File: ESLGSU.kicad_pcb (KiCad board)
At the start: 2 copper layers, 1 part

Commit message: Started work on system power section
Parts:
- added C1: 1n, Capacitor_SMD:C_0603_1608Metric, F.Cu at (144.4, 69.7)
- added C10: 100n, Capacitor_SMD:C_0603_1608Metric, F.Cu at (167.1, 69.5)
- added C11: 100n, Capacitor_SMD:C_0603_1608Metric, F.Cu at (171.1, 62.0)
- added C2: 1u, Capacitor_SMD:C_0603_1608Metric, F.Cu at (144.4, 72.2)
- added C3: 22n, Capacitor_SMD:C_0603_1608Metric, F.Cu at (163.1, 62.0)
- added C4: 100n, Capacitor_SMD:C_0603_1608Metric, F.Cu at (163.1, 64.5)
- added C5: 100n, Capacitor_SMD:C_0603_1608Metric, F.Cu at (163.1, 67.0)
- added C6: 100n, Capacitor_SMD:C_0603_1608Metric, F.Cu at (163.1, 69.5)
- added C7: 1u, Capacitor_SMD:C_0603_1608Metric, F.Cu at (167.1, 62.0)
- added C8: 1n, Capacitor_SMD:C_0603_1608Metric, F.Cu at (167.1, 64.5)
- added C9: 22n, Capacitor_SMD:C_0603_1608Metric, F.Cu at (167.1, 67.0)
- added R1: 10K, Resistor_SMD:R_0603_1608Metric, F.Cu at (171.1, 64.5)
- added R2: 5m, Resistor_SMD:R_0603_1608Metric, F.Cu at (171.1, 67.0)
- added R3: 10K, Resistor_SMD:R_0603_1608Metric, F.Cu at (171.1, 69.5)
- added U2: DML3012LDC, Package_DFN_QFN:WDFN-12-1EP_3x3mm_P0.45mm_EP1.7x2.5mm, F.Cu at (149.0, 70.8)
- added U3: LM74700, Package_TO_SOT_SMD:SOT-23-6, F.Cu at (158.5, 63.0)
- added U4: ~, ESLGSU_Parts_Lib:V-DFN3030-8, F.Cu at (163.3, 73.0)
- added U5: INA219AxDCN, Package_TO_SOT_SMD:SOT-23-8, F.Cu at (158.5, 67.4)
- added U6: DML3012LDC, Package_DFN_QFN:WDFN-12-1EP_3x3mm_P0.45mm_EP1.7x2.5mm, F.Cu at (168.2, 73.0)
- added U7: ~, ESLGSU_Parts_Lib:V-DFN3030-8, F.Cu at (163.3, 77.6)
- added U8: LM74700, Package_TO_SOT_SMD:SOT-23-6, F.Cu at (158.5, 71.9)
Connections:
- U1 pad 11: /Pi_Zero/PI_SS_MISC2_IO2 -> /Pi_Zero/PI_RESET_MAIN
- U1 pad 12: unconnected-(U1-GPIO18-Pad12) -> /Pi_Zero/PI_BOOT0_MAIN
- U1 pad 13: /Pi_Zero/PI_RESET_MISC2_IO4 -> /Pi_Zero/PI_BOOT0_MISC2_IO6
- U1 pad 15: /Pi_Zero/PI_BOOT0_MISC2_IO6 -> /Pi_Zero/PI_SS_MISC1_IO1
- U1 pad 16: unconnected-(U1-GPIO23-Pad16) -> /Pi_Zero/PI_RESET_MISC1_IO3
- U1 pad 18: unconnected-(U1-GPIO24-Pad18) -> /Pi_Zero/PI_BOOT0_MISC1_IO5
- U1 pad 22: /Pi_Zero/PI_SS_MISC1_IO1 -> /Pi_Zero/PI_SS_MISC2_IO2
- U1 pad 24: /Pi_Zero/PI_RESET_MISC1_IO3 -> unconnected-(U1-GPIO8-Pad24)
- U1 pad 26: /Pi_Zero/PI_BOOT0_MISC1_IO5 -> unconnected-(U1-GPIO7-Pad26)
- U1 pad 33: /Pi_Zero/PI_SS_MAIN -> unconnected-(U1-GPIO13_PWM1-Pad33)
- U1 pad 35: /Pi_Zero/PI_RESET_MAIN -> /Pi_Zero/PI_SS_EPS
- U1 pad 36: /Pi_Zero/PI_SS_EPS -> /Pi_Zero/PI_SS_MAIN
- U1 pad 37: /Pi_Zero/PI_BOOT0_MAIN -> /Pi_Zero/PI_RESET_MISC2_IO4

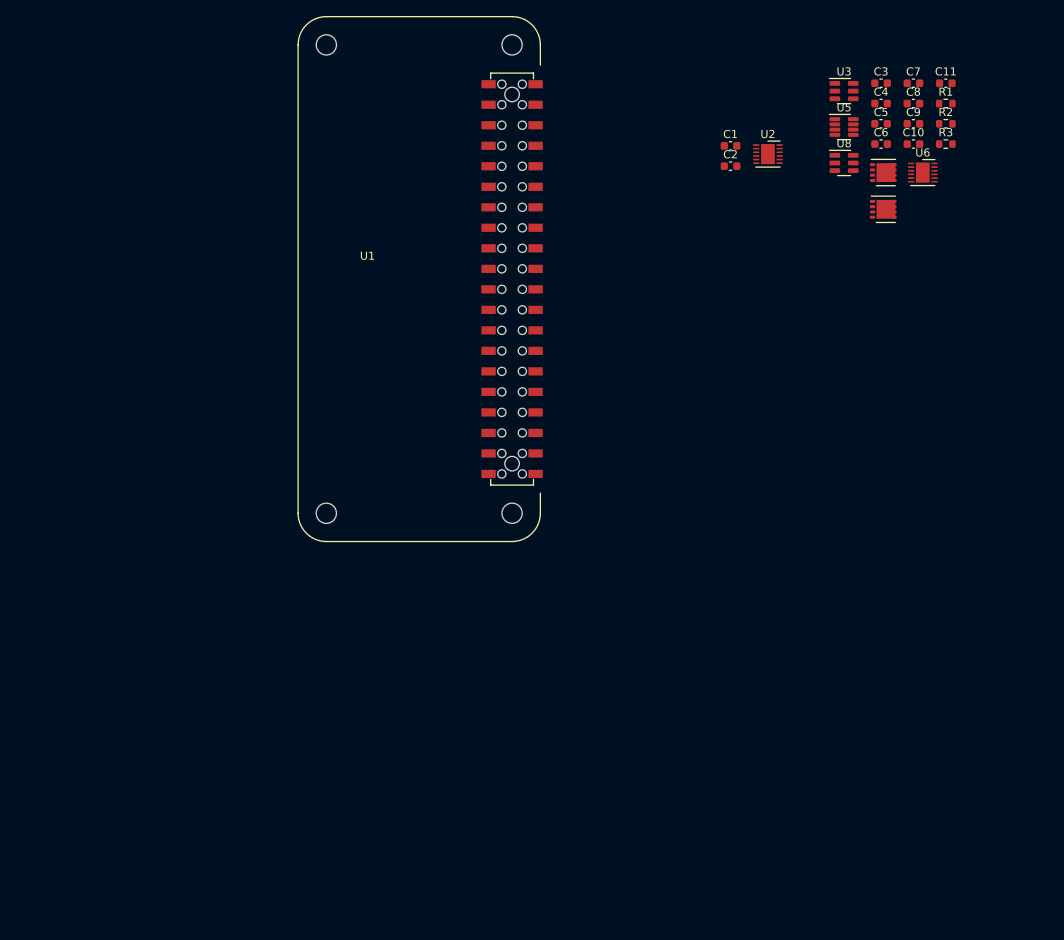
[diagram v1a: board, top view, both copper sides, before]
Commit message: Additional power regulation work
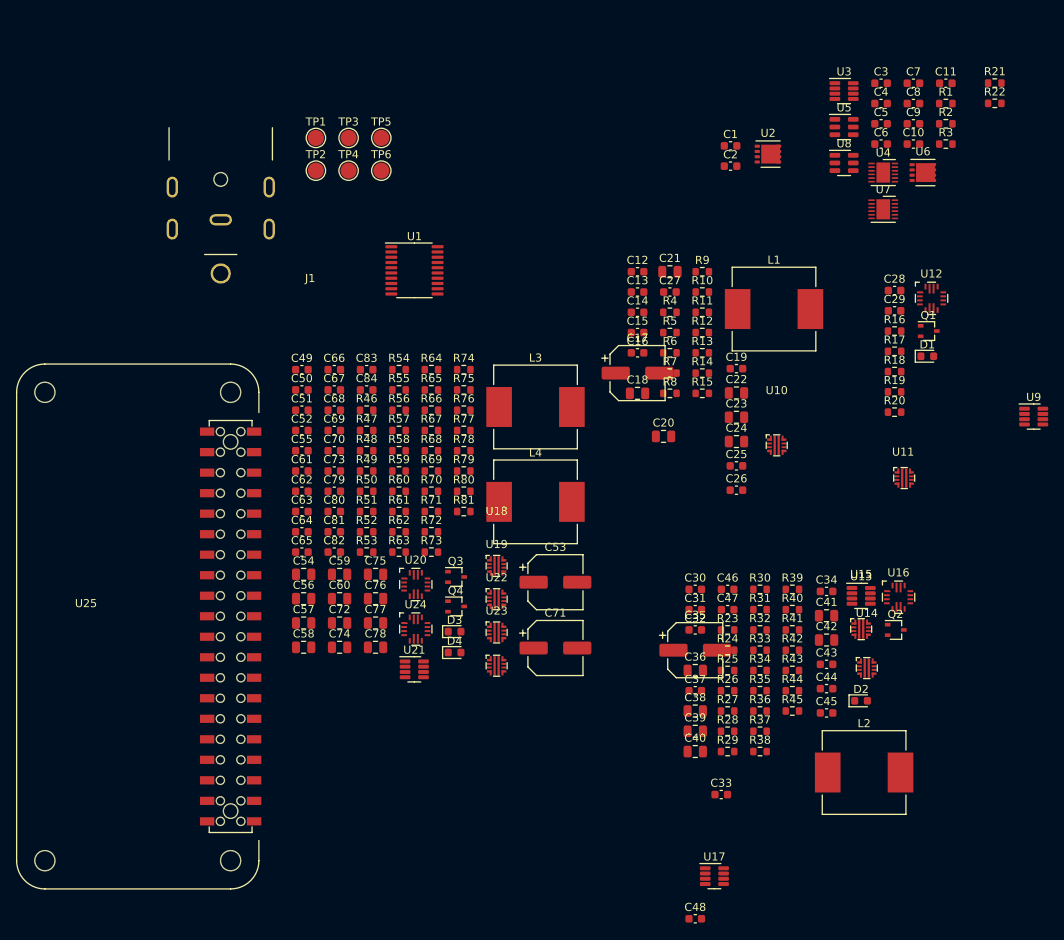
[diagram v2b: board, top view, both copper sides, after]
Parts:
- added C12: 100n, Capacitor_SMD:C_0603_1608Metric, F.Cu at (132.9, 85.3)
- added C13: 100n, Capacitor_SMD:C_0603_1608Metric, F.Cu at (132.9, 87.8)
- added C14: 100n, Capacitor_SMD:C_0603_1608Metric, F.Cu at (132.9, 90.3)
- added C15: 100n, Capacitor_SMD:C_0603_1608Metric, F.Cu at (132.9, 92.9)
- added C16: 100n, Capacitor_SMD:C_0603_1608Metric, F.Cu at (132.9, 95.4)
- added C17: 100u, Capacitor_SMD:CP_Elec_6.3x7.7, F.Cu at (132.9, 97.9)
- added C18: 22u, Capacitor_SMD:C_0805_2012Metric, F.Cu at (132.9, 100.4)
- added C19: 22n, Capacitor_SMD:C_0603_1608Metric, F.Cu at (145.1, 97.3)
- added C20: 22u, Capacitor_SMD:C_0805_2012Metric, F.Cu at (136.1, 105.7)
- added C21: 22u, Capacitor_SMD:C_0805_2012Metric, F.Cu at (136.9, 85.3)
- added C22: 22u, Capacitor_SMD:C_0805_2012Metric, F.Cu at (145.1, 100.3)
- added C23: 22u, Capacitor_SMD:C_0805_2012Metric, F.Cu at (145.1, 103.3)
- added C24: 22u, Capacitor_SMD:C_0805_2012Metric, F.Cu at (145.1, 106.4)
- added C25: 100n, Capacitor_SMD:C_0603_1608Metric, F.Cu at (145.1, 109.4)
- added C26: 1u, Capacitor_SMD:C_0603_1608Metric, F.Cu at (145.1, 112.4)
- added C27: 330p, Capacitor_SMD:C_0603_1608Metric, F.Cu at (136.9, 87.8)
- added C28: 2.2n, Capacitor_SMD:C_0603_1608Metric, F.Cu at (164.7, 87.7)
- added C29: 1u, Capacitor_SMD:C_0603_1608Metric, F.Cu at (164.7, 90.2)
- added C30: 1u, Capacitor_SMD:C_0603_1608Metric, F.Cu at (140.0, 124.7)
- added C31: 100n, Capacitor_SMD:C_0603_1608Metric, F.Cu at (140.0, 127.2)
- added C32: 100n, Capacitor_SMD:C_0603_1608Metric, F.Cu at (140.0, 129.7)
- added C33: 100n, Capacitor_SMD:C_0603_1608Metric, F.Cu at (143.3, 150.1)
- added C34: 100n, Capacitor_SMD:C_0603_1608Metric, F.Cu at (156.3, 124.9)
- added C35: 100u, Capacitor_SMD:CP_Elec_6.3x7.7, F.Cu at (140.0, 132.2)
- added C36: 22u, Capacitor_SMD:C_0805_2012Metric, F.Cu at (140.0, 134.7)
- added C37: 22n, Capacitor_SMD:C_0603_1608Metric, F.Cu at (140.0, 137.2)
- added C38: 22u, Capacitor_SMD:C_0805_2012Metric, F.Cu at (140.0, 139.7)
- added C39: 22u, Capacitor_SMD:C_0805_2012Metric, F.Cu at (140.0, 142.2)
- added C40: 22u, Capacitor_SMD:C_0805_2012Metric, F.Cu at (140.0, 144.7)
- added C41: 22u, Capacitor_SMD:C_0805_2012Metric, F.Cu at (156.3, 127.9)
- added C42: 22u, Capacitor_SMD:C_0805_2012Metric, F.Cu at (156.3, 130.9)
- added C43: 100n, Capacitor_SMD:C_0603_1608Metric, F.Cu at (156.3, 133.9)
- added C44: 1u, Capacitor_SMD:C_0603_1608Metric, F.Cu at (156.3, 136.9)
- added C45: 330p, Capacitor_SMD:C_0603_1608Metric, F.Cu at (156.3, 140.0)
- added C46: 2.2n, Capacitor_SMD:C_0603_1608Metric, F.Cu at (144.1, 124.7)
- added C47: 1u, Capacitor_SMD:C_0603_1608Metric, F.Cu at (144.1, 127.2)
- added C48: 1u, Capacitor_SMD:C_0603_1608Metric, F.Cu at (140.0, 165.4)
- added C49: 100n, Capacitor_SMD:C_0603_1608Metric, F.Cu at (91.3, 97.5)
- added C50: 100n, Capacitor_SMD:C_0603_1608Metric, F.Cu at (91.3, 100.0)
- added C51: 100n, Capacitor_SMD:C_0603_1608Metric, F.Cu at (91.3, 102.5)
- added C52: 100n, Capacitor_SMD:C_0603_1608Metric, F.Cu at (91.3, 105.0)
- added C53: 100u, Capacitor_SMD:CP_Elec_6.3x7.7, F.Cu at (122.7, 123.8)
- added C54: 22u, Capacitor_SMD:C_0805_2012Metric, F.Cu at (91.5, 122.8)
- added C55: 22n, Capacitor_SMD:C_0603_1608Metric, F.Cu at (91.3, 107.5)
- added C56: 22u, Capacitor_SMD:C_0805_2012Metric, F.Cu at (91.5, 125.8)
- added C57: 22u, Capacitor_SMD:C_0805_2012Metric, F.Cu at (91.5, 128.8)
- added C58: 22u, Capacitor_SMD:C_0805_2012Metric, F.Cu at (91.5, 131.8)
- added C59: 22u, Capacitor_SMD:C_0805_2012Metric, F.Cu at (96.0, 122.8)
- added C60: 22u, Capacitor_SMD:C_0805_2012Metric, F.Cu at (96.0, 125.8)
- added C61: 100n, Capacitor_SMD:C_0603_1608Metric, F.Cu at (91.3, 110.0)
- added C62: 1u, Capacitor_SMD:C_0603_1608Metric, F.Cu at (91.3, 112.5)
- added C63: 330p, Capacitor_SMD:C_0603_1608Metric, F.Cu at (91.3, 115.0)
- added C64: 2.2n, Capacitor_SMD:C_0603_1608Metric, F.Cu at (91.3, 117.5)
- added C65: 1u, Capacitor_SMD:C_0603_1608Metric, F.Cu at (91.3, 120.0)
- added C66: 1u, Capacitor_SMD:C_0603_1608Metric, F.Cu at (95.3, 97.5)
- added C67: 100n, Capacitor_SMD:C_0603_1608Metric, F.Cu at (95.3, 100.0)
- added C68: 100n, Capacitor_SMD:C_0603_1608Metric, F.Cu at (95.3, 102.5)
- added C69: 100n, Capacitor_SMD:C_0603_1608Metric, F.Cu at (95.3, 105.0)
- added C70: 100n, Capacitor_SMD:C_0603_1608Metric, F.Cu at (95.3, 107.5)
- added C71: 100u, Capacitor_SMD:CP_Elec_6.3x7.7, F.Cu at (122.7, 131.9)
- added C72: 22u, Capacitor_SMD:C_0805_2012Metric, F.Cu at (96.0, 128.8)
- added C73: 22n, Capacitor_SMD:C_0603_1608Metric, F.Cu at (95.3, 110.0)
- added C74: 22u, Capacitor_SMD:C_0805_2012Metric, F.Cu at (96.0, 131.8)
- added C75: 22u, Capacitor_SMD:C_0805_2012Metric, F.Cu at (100.5, 122.8)
- added C76: 22u, Capacitor_SMD:C_0805_2012Metric, F.Cu at (100.5, 125.8)
- added C77: 22u, Capacitor_SMD:C_0805_2012Metric, F.Cu at (100.5, 128.8)
- added C78: 22u, Capacitor_SMD:C_0805_2012Metric, F.Cu at (100.5, 131.8)
- added C79: 100n, Capacitor_SMD:C_0603_1608Metric, F.Cu at (95.3, 112.5)
- added C80: 1u, Capacitor_SMD:C_0603_1608Metric, F.Cu at (95.3, 115.0)
- added C81: 330p, Capacitor_SMD:C_0603_1608Metric, F.Cu at (95.3, 117.5)
- added C82: 2.2n, Capacitor_SMD:C_0603_1608Metric, F.Cu at (95.3, 120.0)
- added C83: 1u, Capacitor_SMD:C_0603_1608Metric, F.Cu at (99.3, 97.5)
- added C84: 1u, Capacitor_SMD:C_0603_1608Metric, F.Cu at (99.3, 100.0)
- added D1: LED, LED_SMD:LED_0603_1608Metric, F.Cu at (168.8, 95.8)
- added D2: LED, LED_SMD:LED_0603_1608Metric, F.Cu at (160.6, 138.5)
- added D3: LED, LED_SMD:LED_0603_1608Metric, F.Cu at (110.2, 129.9)
- added D4: LED, LED_SMD:LED_0603_1608Metric, F.Cu at (110.2, 132.5)
- added J1: Barrel_Jack_Switch, ESLGSU_Parts_Lib:PJ-082BH, F.Cu at (81.3, 67.5)
- added L1: IHLP4040DZER4R7M01, Inductor_SMD:L_Vishay_IHLP-4040, F.Cu at (149.8, 89.9)
- added L2: IHLP4040DZER4R7M01, Inductor_SMD:L_Vishay_IHLP-4040, F.Cu at (161.0, 147.3)
- added L3: IHLP4040DZER4R7M01, Inductor_SMD:L_Vishay_IHLP-4040, F.Cu at (120.3, 102.1)
- added L4: IHLP4040DZER4R7M01, Inductor_SMD:L_Vishay_IHLP-4040, F.Cu at (120.3, 113.8)
- added Q1: DMN67D7L-7, Package_TO_SOT_SMD:SOT-323_SC-70, F.Cu at (169.0, 92.7)
- added Q2: DMN67D7L-7, Package_TO_SOT_SMD:SOT-323_SC-70, F.Cu at (164.9, 129.7)
- added Q3: DMN67D7L-7, Package_TO_SOT_SMD:SOT-323_SC-70, F.Cu at (110.4, 123.1)
- added Q4: DMN67D7L-7, Package_TO_SOT_SMD:SOT-323_SC-70, F.Cu at (110.4, 126.8)
- added R10: 47K, Resistor_SMD:R_0603_1608Metric, F.Cu at (140.9, 87.8)
- added R11: 430K, Resistor_SMD:R_0603_1608Metric, F.Cu at (140.9, 90.3)
- added R12: 31.6K, Resistor_SMD:R_0603_1608Metric, F.Cu at (140.9, 92.9)
- added R13: 5m, Resistor_SMD:R_0603_1608Metric, F.Cu at (140.9, 95.4)
- added R14: 17.4K, Resistor_SMD:R_0603_1608Metric, F.Cu at (140.9, 97.9)
- added R15: 806K, Resistor_SMD:R_0603_1608Metric, F.Cu at (140.9, 100.4)
- added R16: 3.74K, Resistor_SMD:R_0603_1608Metric, F.Cu at (164.7, 92.7)
- added R17: 14.7K, Resistor_SMD:R_0603_1608Metric, F.Cu at (164.7, 95.2)
- added R18: 187K, Resistor_SMD:R_0603_1608Metric, F.Cu at (164.7, 97.7)
- added R19: 7.5K, Resistor_SMD:R_0603_1608Metric, F.Cu at (164.7, 100.2)
- added R20: 16.9K, Resistor_SMD:R_0603_1608Metric, F.Cu at (164.7, 102.7)
- added R21: 21.5K, Resistor_SMD:R_0603_1608Metric, F.Cu at (177.1, 62.0)
- added R22: 549R, Resistor_SMD:R_0603_1608Metric, F.Cu at (177.1, 64.5)
- added R23: 0R, Resistor_SMD:R_0603_1608Metric, F.Cu at (144.1, 129.7)
- added R24: 0R, Resistor_SMD:R_0603_1608Metric, F.Cu at (144.1, 132.2)
- added R25: 100R, Resistor_SMD:R_0603_1608Metric, F.Cu at (144.1, 134.7)
- added R26: 100K, Resistor_SMD:R_0603_1608Metric, F.Cu at (144.1, 137.2)
- added R27: 47K, Resistor_SMD:R_0603_1608Metric, F.Cu at (144.1, 139.7)
- added R28: 430K, Resistor_SMD:R_0603_1608Metric, F.Cu at (144.1, 142.2)
- added R29: 31.6K, Resistor_SMD:R_0603_1608Metric, F.Cu at (144.1, 144.7)
- added R30: 5m, Resistor_SMD:R_0603_1608Metric, F.Cu at (148.1, 124.7)
- added R31: 17.4K, Resistor_SMD:R_0603_1608Metric, F.Cu at (148.1, 127.2)
- added R32: 806K, Resistor_SMD:R_0603_1608Metric, F.Cu at (148.1, 129.7)
- added R33: 2.09K, Resistor_SMD:R_0603_1608Metric, F.Cu at (148.1, 132.2)
- added R34: 14.7K, Resistor_SMD:R_0603_1608Metric, F.Cu at (148.1, 134.7)
- added R35: 107K, Resistor_SMD:R_0603_1608Metric, F.Cu at (148.1, 137.2)
- added R36: 7.5K, Resistor_SMD:R_0603_1608Metric, F.Cu at (148.1, 139.7)
- added R37: 9.09K, Resistor_SMD:R_0603_1608Metric, F.Cu at (148.1, 142.2)
- added R38: 21.5K, Resistor_SMD:R_0603_1608Metric, F.Cu at (148.1, 144.7)
- added R39: 549R, Resistor_SMD:R_0603_1608Metric, F.Cu at (152.1, 124.7)
- added R4: 10K, Resistor_SMD:R_0603_1608Metric, F.Cu at (136.9, 90.3)
- added R40: 4.7K, Resistor_SMD:R_0603_1608Metric, F.Cu at (152.1, 127.2)
- added R41: 4.7K, Resistor_SMD:R_0603_1608Metric, F.Cu at (152.1, 129.7)
- added R42: 4.7K, Resistor_SMD:R_0603_1608Metric, F.Cu at (152.1, 132.2)
- added R43: 4.7K, Resistor_SMD:R_0603_1608Metric, F.Cu at (152.1, 134.7)
- added R44: 4.7K, Resistor_SMD:R_0603_1608Metric, F.Cu at (152.1, 137.2)
- added R45: 4.7K, Resistor_SMD:R_0603_1608Metric, F.Cu at (152.1, 139.7)
- added R46: 0R, Resistor_SMD:R_0603_1608Metric, F.Cu at (99.3, 102.5)
- added R47: 0R, Resistor_SMD:R_0603_1608Metric, F.Cu at (99.3, 105.0)
- added R48: 100R, Resistor_SMD:R_0603_1608Metric, F.Cu at (99.3, 107.5)
- added R49: 100K, Resistor_SMD:R_0603_1608Metric, F.Cu at (99.3, 110.0)
- added R5: 100R, Resistor_SMD:R_0603_1608Metric, F.Cu at (136.9, 92.9)
- added R50: 47K, Resistor_SMD:R_0603_1608Metric, F.Cu at (99.3, 112.5)
- added R51: 430K, Resistor_SMD:R_0603_1608Metric, F.Cu at (99.3, 115.0)
- added R52: 350K, Resistor_SMD:R_0603_1608Metric, F.Cu at (99.3, 117.5)
- added R53: 5m, Resistor_SMD:R_0603_1608Metric, F.Cu at (99.3, 120.0)
- added R54: 17.4K, Resistor_SMD:R_0603_1608Metric, F.Cu at (103.4, 97.5)
- added R55: 806K, Resistor_SMD:R_0603_1608Metric, F.Cu at (103.4, 100.0)
- added R56: 14.7K, Resistor_SMD:R_0603_1608Metric, F.Cu at (103.4, 102.5)
- added R57: 187K, Resistor_SMD:R_0603_1608Metric, F.Cu at (103.4, 105.0)
- added R58: 7.5K, Resistor_SMD:R_0603_1608Metric, F.Cu at (103.4, 107.5)
- added R59: 21.5K, Resistor_SMD:R_0603_1608Metric, F.Cu at (103.4, 110.0)
- added R6: 0R, Resistor_SMD:R_0603_1608Metric, F.Cu at (136.9, 95.4)
- added R60: 549R, Resistor_SMD:R_0603_1608Metric, F.Cu at (103.4, 112.5)
- added R61: 0R, Resistor_SMD:R_0603_1608Metric, F.Cu at (103.4, 115.0)
- added R62: 0R, Resistor_SMD:R_0603_1608Metric, F.Cu at (103.4, 117.5)
- added R63: 100R, Resistor_SMD:R_0603_1608Metric, F.Cu at (103.4, 120.0)
- added R64: 100K, Resistor_SMD:R_0603_1608Metric, F.Cu at (107.4, 97.5)
- added R65: 47K, Resistor_SMD:R_0603_1608Metric, F.Cu at (107.4, 100.0)
- added R66: 430K, Resistor_SMD:R_0603_1608Metric, F.Cu at (107.4, 102.5)
- added R67: 350K, Resistor_SMD:R_0603_1608Metric, F.Cu at (107.4, 105.0)
- added R68: 5m, Resistor_SMD:R_0603_1608Metric, F.Cu at (107.4, 107.5)
- added R69: 17.4K, Resistor_SMD:R_0603_1608Metric, F.Cu at (107.4, 110.0)
- added R7: 0R, Resistor_SMD:R_0603_1608Metric, F.Cu at (136.9, 97.9)
- added R70: 806K, Resistor_SMD:R_0603_1608Metric, F.Cu at (107.4, 112.5)
- added R71: 14.7K, Resistor_SMD:R_0603_1608Metric, F.Cu at (107.4, 115.0)
- added R72: 107K, Resistor_SMD:R_0603_1608Metric, F.Cu at (107.4, 117.5)
- added R73: 7.5K, Resistor_SMD:R_0603_1608Metric, F.Cu at (107.4, 120.0)
- added R74: 21.5K, Resistor_SMD:R_0603_1608Metric, F.Cu at (111.4, 97.5)
- added R75: 549R, Resistor_SMD:R_0603_1608Metric, F.Cu at (111.4, 100.0)
- added R76: 4.7K, Resistor_SMD:R_0603_1608Metric, F.Cu at (111.4, 102.5)
- added R77: 4.7K, Resistor_SMD:R_0603_1608Metric, F.Cu at (111.4, 105.0)
- added R78: 4.7K, Resistor_SMD:R_0603_1608Metric, F.Cu at (111.4, 107.5)
- added R79: 4.7K, Resistor_SMD:R_0603_1608Metric, F.Cu at (111.4, 110.0)
- added R8: 100R, Resistor_SMD:R_0603_1608Metric, F.Cu at (136.9, 100.4)
- added R80: 4.7K, Resistor_SMD:R_0603_1608Metric, F.Cu at (111.4, 112.5)
- added R81: 4.7K, Resistor_SMD:R_0603_1608Metric, F.Cu at (111.4, 115.0)
- added R9: 100K, Resistor_SMD:R_0603_1608Metric, F.Cu at (140.9, 85.3)
- added TP1: TestPoint, TestPoint:TestPoint_Pad_D2.0mm, F.Cu at (93.1, 68.8)
- added TP2: TestPoint, TestPoint:TestPoint_Pad_D2.0mm, F.Cu at (93.1, 72.8)
- added TP3: TestPoint, TestPoint:TestPoint_Pad_D2.0mm, F.Cu at (97.1, 68.8)
- added TP4: TestPoint, TestPoint:TestPoint_Pad_D2.0mm, F.Cu at (97.1, 72.8)
- added TP5: TestPoint, TestPoint:TestPoint_Pad_D2.0mm, F.Cu at (101.2, 68.8)
- added TP6: TestPoint, TestPoint:TestPoint_Pad_D2.0mm, F.Cu at (101.2, 72.8)
- added U10: TPS259474LRPWR, ESLGSU_Parts_Lib:VQFN-HR, F.Cu at (150.1, 106.8)
- added U11: LM73100RPWR, ESLGSU_Parts_Lib:VQFN-HR, F.Cu at (165.9, 110.9)
- added U12: MP28167-A, ESLGSU_Parts_Lib:QFN-16-MP28167, F.Cu at (169.3, 88.6)
- added U13: INA219AxDCN, Package_TO_SOT_SMD:SOT-23-8, F.Cu at (160.6, 125.5)
- added U14: TPS259474LRPWR, ESLGSU_Parts_Lib:VQFN-HR, F.Cu at (161.3, 134.4)
- added U15: LM73100RPWR, ESLGSU_Parts_Lib:VQFN-HR, F.Cu at (160.6, 129.6)
- added U16: MP28167-A, ESLGSU_Parts_Lib:QFN-16-MP28167, F.Cu at (165.2, 125.6)
- added U17: INA219AxDCN, Package_TO_SOT_SMD:SOT-23-8, F.Cu at (142.4, 160.2)
- added U18: TPS259474LRPWR, ESLGSU_Parts_Lib:VQFN-HR, F.Cu at (115.4, 121.8)
- added U19: LM73100RPWR, ESLGSU_Parts_Lib:VQFN-HR, F.Cu at (115.4, 125.9)
- added U20: MP28167-A, ESLGSU_Parts_Lib:QFN-16-MP28167, F.Cu at (105.4, 124.1)
- added U21: INA219AxDCN, Package_TO_SOT_SMD:SOT-23-8, F.Cu at (105.2, 134.6)
- added U22: TPS259474LRPWR, ESLGSU_Parts_Lib:VQFN-HR, F.Cu at (115.4, 130.0)
- added U23: LM73100RPWR, ESLGSU_Parts_Lib:VQFN-HR, F.Cu at (115.4, 134.1)
- added U24: MP28167-A, ESLGSU_Parts_Lib:QFN-16-MP28167, F.Cu at (105.4, 129.6)
- added U25: ~, ESLGSU_Parts_Lib:PI_ZERO_2_W, F.Cu at (70.4, 128.2)
- added U9: INA219AxDCN, Package_TO_SOT_SMD:SOT-23-8, F.Cu at (181.9, 103.3)
- C1: value 1n -> 100n
- C11, C6: value 100n -> 1n
- C3: value 22n -> 100n
- C4: value 100n -> 22n
- C7: value 1u -> 100n
- C8: value 1n -> 1u
- R2: value 5m -> 100R
- R3: value 10K -> 5m
- U1: value ~ -> TCA9544A; footprint ESLGSU_Parts_Lib:PI_ZERO_2_W -> Package_SO:TSSOP-20_4.4x6.5mm_P0.65mm
- U2, U6: value DML3012LDC -> DMT3006LDK; footprint Package_DFN_QFN:WDFN-12-1EP_3x3mm_P0.45mm_EP1.7x2.5mm -> ESLGSU_Parts_Lib:V-DFN3030-8
- U3: value LM74700 -> INA219AxDCN; footprint Package_TO_SOT_SMD:SOT-23-6 -> Package_TO_SOT_SMD:SOT-23-8
- U4, U7: value ~ -> DML3012LDC; footprint ESLGSU_Parts_Lib:V-DFN3030-8 -> Package_DFN_QFN:WDFN-12-1EP_3x3mm_P0.45mm_EP1.7x2.5mm
- U5: value INA219AxDCN -> LM74700; footprint Package_TO_SOT_SMD:SOT-23-8 -> Package_TO_SOT_SMD:SOT-23-6
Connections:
- C1 pad 1: Net-(U2-SR) -> /SYS_3V3
- C1 pad 2: GNDA -> GND
- C10 pad 1: Net-(U8-VCAP) -> Net-(U2-D)
- C11 pad 1: Net-(U3-CATHODE) -> Net-(U7-SR)
- C2 pad 1: Net-(U2-VCC) -> Net-(U4-VCC)
- C3 pad 1: Net-(U3-ANODE) -> Net-(U3-VS)
- C3 pad 2: GNDA -> GND
- C4 pad 1: Net-(U3-CATHODE) -> Net-(U2-S)
- C5 pad 1: Net-(U3-VCAP) -> Net-(U2-D)
- C6 pad 1: Net-(U5-VS) -> Net-(U4-SR)
- C6 pad 2: GND -> GNDA
- C7 pad 1: Net-(U6-VCC) -> Net-(U5-VCAP)
- C8 pad 1: Net-(U6-SR) -> Net-(U7-VCC)
- C9 pad 1: Net-(U7-S) -> Net-(U6-S)
- R1 pad 1: Net-(U2-VCC) -> Net-(U4-VCC)
- R1 pad 2: Net-(U2-PG) -> Net-(U4-PG)
- R2 pad 1: Net-(U3-CATHODE) -> Net-(U4-BLEED)
- R2 pad 2: /System_Power/BUS_UNREG -> Net-(U2-S)
- R3 pad 1: Net-(U6-VCC) -> Net-(U2-D)
- R3 pad 2: Net-(U6-PG) -> /BUS_UNREG
- U1 pad 1: unconnected-(U1-3V3-Pad1) -> GND
- U1 pad 10: /Pi_Zero/PI_UART_RX -> GND
- U1 pad 11: /Pi_Zero/PI_RESET_MAIN -> /Programmable_Regulators/INT_CH1
- U1 pad 12: /Pi_Zero/PI_BOOT0_MAIN -> /Programmable_Regulators/SDA_CH1
- U1 pad 13: /Pi_Zero/PI_BOOT0_MISC2_IO6 -> /Programmable_Regulators/SCL_CH1
- U1 pad 14: GND -> /Programmable_Regulators/INT_CH2
- U1 pad 15: /Pi_Zero/PI_SS_MISC1_IO1 -> /Programmable_Regulators/SDA_CH2
- U1 pad 16: /Pi_Zero/PI_RESET_MISC1_IO3 -> /Programmable_Regulators/SCL_CH2
- U1 pad 17: unconnected-(U1-3V3-Pad17) -> /EPS_INT
- U1 pad 18: /Pi_Zero/PI_BOOT0_MISC1_IO5 -> /EPS_SCL
- U1 pad 19: /Pi_Zero/PI_MOSI -> /EPS_SDA
- U1 pad 2: /SYS_5V -> GND
- U1 pad 20: GND -> /SYS_3V3
- U1 pad 3: /Pi_Zero/PI_I2C_SDA -> GND
- U1 pad 4: /SYS_5V -> /Fixed_Regulators/INT_5V
- U1 pad 5: /Pi_Zero/PI_I2C_SCL -> /Fixed_Regulators/SDA_5V
- U1 pad 6: GND -> /Fixed_Regulators/SCL_5V
- U1 pad 7: unconnected-(U1-GPIO4-Pad7) -> /Fixed_Regulators/INT_3V3
- U1 pad 8: /Pi_Zero/PI_UART_TX -> /Fixed_Regulators/SDA_3V3
- U1 pad 9: GND -> /Fixed_Regulators/SCL_3V3
- U2 pad 1: /System_Power/POWER_IN -> Net-(U2-G)
- U2 pad 2: /System_Power/EN_P_IN_UNREG -> Net-(U2-S)
- U2 pad 3: Net-(U2-VCC) -> Net-(U2-D)
- U3 pad 1: Net-(U3-VCAP) -> Net-(U2-D)
- U3 pad 2: GNDA -> /BUS_UNREG
- U3 pad 3: Net-(U2-PG) -> GND
- U3 pad 4: Net-(U3-CATHODE) -> Net-(U3-VS)
- U3 pad 5: Net-(U3-GATE) -> /EPS_SCL
- U3 pad 6: Net-(U3-ANODE) -> /EPS_SDA
- U4 pad 1: Net-(U3-GATE) -> /System_Power/POWER_IN
- U4 pad 2: Net-(U3-ANODE) -> /System_Power/EN_P_IN_UNREG
- U4 pad 3: Net-(U3-CATHODE) -> Net-(U4-VCC)
- U5 pad 1: Net-(U3-CATHODE) -> Net-(U5-VCAP)
- U5 pad 2: /System_Power/BUS_UNREG -> GNDA
- U5 pad 3: GND -> Net-(U4-PG)
- U5 pad 4: Net-(U5-VS) -> Net-(U2-D)
- U5 pad 5: /System_Power/EPS_SCL -> Net-(U2-G)
- U5 pad 6: /System_Power/EPS_SDA -> Net-(U2-S)
- U6 pad 1: Net-(U6-VIN-Pad1) -> Net-(U6-G)
- U6 pad 2: /System_Power/EN_BAT_UNREG -> Net-(U6-S)
- U6 pad 3: Net-(U6-VCC) -> Net-(U2-D)
- U7 pad 1: Net-(U7-G) -> Net-(U7-VIN-Pad1)
- U7 pad 2: Net-(U7-S) -> /System_Power/EN_BAT_UNREG
- U7 pad 3: Net-(U3-CATHODE) -> Net-(U7-VCC)
- U8 pad 3: Net-(U6-PG) -> Net-(U7-PG)
- U8 pad 4: Net-(U3-CATHODE) -> Net-(U2-D)
- U8 pad 5: Net-(U7-G) -> Net-(U6-G)
- U8 pad 6: Net-(U7-S) -> Net-(U6-S)

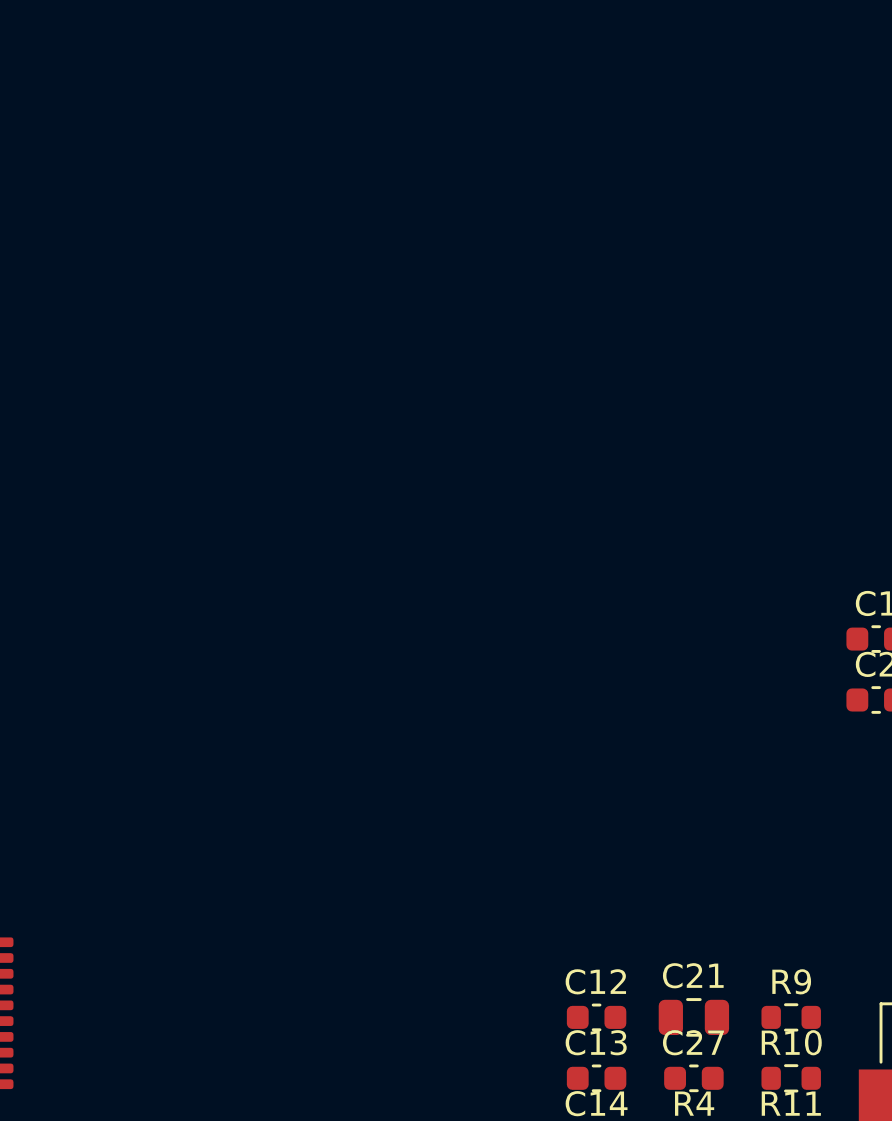
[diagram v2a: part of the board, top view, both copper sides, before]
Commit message: Added 5v/3V3 regulators and mux
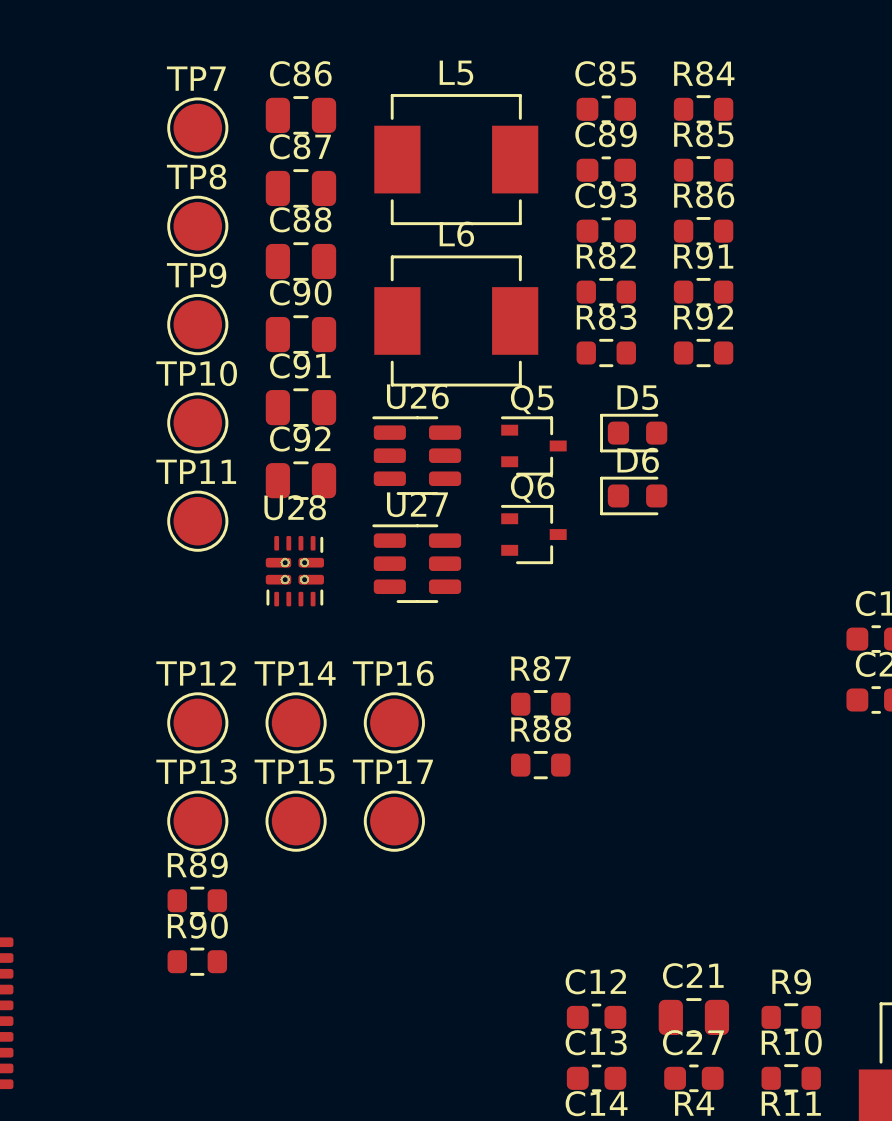
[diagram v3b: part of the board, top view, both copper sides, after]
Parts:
- added C85: 100n, Capacitor_SMD:C_0603_1608Metric, F.Cu at (133.3, 47.9)
- added C86: 22u, Capacitor_SMD:C_0805_2012Metric, F.Cu at (120.7, 48.2)
- added C87: 22u, Capacitor_SMD:C_0805_2012Metric, F.Cu at (120.7, 51.2)
- added C88: 10u, Capacitor_SMD:C_0805_2012Metric, F.Cu at (120.7, 54.2)
- added C89: 100n, Capacitor_SMD:C_0603_1608Metric, F.Cu at (133.3, 50.4)
- added C90: 22u, Capacitor_SMD:C_0805_2012Metric, F.Cu at (120.7, 57.2)
- added C91: 22u, Capacitor_SMD:C_0805_2012Metric, F.Cu at (120.7, 60.2)
- added C92: 10u, Capacitor_SMD:C_0805_2012Metric, F.Cu at (120.7, 63.2)
- added C93: 100n, Capacitor_SMD:C_0603_1608Metric, F.Cu at (133.3, 52.9)
- added D5: LED, LED_SMD:LED_0603_1608Metric, F.Cu at (134.6, 61.2)
- added D6: LED, LED_SMD:LED_0603_1608Metric, F.Cu at (134.6, 63.8)
- added L5: IHLP2020CZER4R7M11, Inductor_SMD:L_Vishay_IHLP-2020, F.Cu at (127.1, 50.0)
- added L6: IHLP2020CZER4R7M11, Inductor_SMD:L_Vishay_IHLP-2020, F.Cu at (127.1, 56.6)
- added Q5: DMN67D7L-7, Package_TO_SOT_SMD:SOT-323_SC-70, F.Cu at (130.3, 61.8)
- added Q6: DMN67D7L-7, Package_TO_SOT_SMD:SOT-323_SC-70, F.Cu at (130.3, 65.4)
- added R82: 25.5K, Resistor_SMD:R_0603_1608Metric, F.Cu at (133.3, 55.4)
- added R83: 100K, Resistor_SMD:R_0603_1608Metric, F.Cu at (133.3, 58.0)
- added R84: 5.6K, Resistor_SMD:R_0603_1608Metric, F.Cu at (137.3, 47.9)
- added R85: 100K, Resistor_SMD:R_0603_1608Metric, F.Cu at (137.3, 50.4)
- added R86: 5.6K, Resistor_SMD:R_0603_1608Metric, F.Cu at (137.3, 52.9)
- added R87: 47K, Resistor_SMD:R_0603_1608Metric, F.Cu at (130.6, 72.4)
- added R88: 47K, Resistor_SMD:R_0603_1608Metric, F.Cu at (130.6, 74.9)
- added R89: 47K, Resistor_SMD:R_0603_1608Metric, F.Cu at (116.4, 80.5)
- added R90: 47K, Resistor_SMD:R_0603_1608Metric, F.Cu at (116.4, 83.0)
- added R91: 150R, Resistor_SMD:R_0603_1608Metric, F.Cu at (137.3, 55.4)
- added R92: 150R, Resistor_SMD:R_0603_1608Metric, F.Cu at (137.3, 58.0)
- added TP10: TestPoint, TestPoint:TestPoint_Pad_D2.0mm, F.Cu at (116.5, 60.8)
- added TP11: TestPoint, TestPoint:TestPoint_Pad_D2.0mm, F.Cu at (116.5, 64.9)
- added TP12: TestPoint, TestPoint:TestPoint_Pad_D2.0mm, F.Cu at (116.5, 73.2)
- added TP13: TestPoint, TestPoint:TestPoint_Pad_D2.0mm, F.Cu at (116.5, 77.2)
- added TP14: TestPoint, TestPoint:TestPoint_Pad_D2.0mm, F.Cu at (120.5, 73.2)
- added TP15: TestPoint, TestPoint:TestPoint_Pad_D2.0mm, F.Cu at (120.5, 77.2)
- added TP16: TestPoint, TestPoint:TestPoint_Pad_D2.0mm, F.Cu at (124.6, 73.2)
- added TP17: TestPoint, TestPoint:TestPoint_Pad_D2.0mm, F.Cu at (124.6, 77.2)
- added TP7: TestPoint, TestPoint:TestPoint_Pad_D2.0mm, F.Cu at (116.5, 48.7)
- added TP8: TestPoint, TestPoint:TestPoint_Pad_D2.0mm, F.Cu at (116.5, 52.7)
- added TP9: TestPoint, TestPoint:TestPoint_Pad_D2.0mm, F.Cu at (116.5, 56.8)
- added U26: AP63203WU, Package_TO_SOT_SMD:TSOT-23-6, F.Cu at (125.5, 62.2)
- added U27: AP63205WU, Package_TO_SOT_SMD:TSOT-23-6, F.Cu at (125.5, 66.6)
- added U28: TPS2121, Package_DFN_QFN:Texas_VQFN-HR-12_2x2.5mm_P0.5mm_ThermalVias, F.Cu at (120.5, 66.9)
- J1: value Barrel_Jack_Switch -> PJ-080BH
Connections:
- net Net-(U7-VIN-Pad1) renamed /System_Power/VBAT
- C2 pad 1: Net-(U4-VCC) -> /SYS_5V
- C3 pad 1: Net-(U3-VS) -> /SYS_3V3
- C8 pad 1: Net-(U7-VCC) -> /SYS_5V
- R1 pad 1: Net-(U4-VCC) -> /SYS_5V
- R4 pad 1: Net-(U7-VCC) -> /SYS_5V
- U3 pad 4: Net-(U3-VS) -> /SYS_3V3
- U4 pad 3: Net-(U4-VCC) -> /SYS_5V
- U7 pad 3: Net-(U7-VCC) -> /SYS_5V

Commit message: uC Interface work
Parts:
- added C100: 100n, Capacitor_SMD:C_0603_1608Metric, F.Cu at (211.8, 72.3)
- added C101: 100n, Capacitor_SMD:C_0603_1608Metric, F.Cu at (211.8, 74.8)
- added C102: 100n, Capacitor_SMD:C_0603_1608Metric, F.Cu at (211.8, 77.3)
- added C94: 100n, Capacitor_SMD:C_0603_1608Metric, F.Cu at (207.8, 72.3)
- added C95: 100n, Capacitor_SMD:C_0603_1608Metric, F.Cu at (207.8, 74.8)
- added C96: 100n, Capacitor_SMD:C_0603_1608Metric, F.Cu at (207.8, 77.3)
- added C97: 100n, Capacitor_SMD:C_0603_1608Metric, F.Cu at (207.8, 79.8)
- added C98: 100n, Capacitor_SMD:C_0603_1608Metric, F.Cu at (207.8, 82.3)
- added C99: 100n, Capacitor_SMD:C_0603_1608Metric, F.Cu at (207.8, 84.8)
- added R100: 0R, Resistor_SMD:R_0603_1608Metric, F.Cu at (215.8, 82.3)
- added R93: 120R, Resistor_SMD:R_0603_1608Metric, F.Cu at (211.8, 79.8)
- added R94: 50R, Resistor_SMD:R_0603_1608Metric, F.Cu at (211.8, 82.3)
- added R95: 0R, Resistor_SMD:R_0603_1608Metric, F.Cu at (220.1, 87.7)
- added R96: 0R, Resistor_SMD:R_0603_1608Metric, F.Cu at (215.8, 72.3)
- added R97: 0R, Resistor_SMD:R_0603_1608Metric, F.Cu at (215.8, 74.8)
- added R98: 0R, Resistor_SMD:R_0603_1608Metric, F.Cu at (215.8, 77.3)
- added R99: 0R, Resistor_SMD:R_0603_1608Metric, F.Cu at (215.8, 79.8)
- added U29: TCAN1051GVDRBRQ, Package_DFN_QFN:DFN-8-1EP_3x3mm_P0.65mm_EP1.55x2.4mm, F.Cu at (220.4, 73.3)
- added U30: THVD1450DRBR, Package_DFN_QFN:DFN-8-1EP_3x3mm_P0.65mm_EP1.55x2.4mm, F.Cu at (220.4, 77.8)
- added U31: TXU0304RUTR, ESLGSU_Parts_Lib:T-UQFN-12, F.Cu at (207.5, 91.5)
- added U32: TS5A23159RSER, Package_DFN_QFN:Texas_UQFN-10_1.5x2mm_P0.5mm, F.Cu at (210.9, 91.5)
- added U33: TXU0202DTTR, ESLGSU_Parts_Lib:SOT833-1-XSON8, F.Cu at (207.0, 87.8)
- added U34: 74LVC2G53GT, ESLGSU_Parts_Lib:SOT833-1-XSON8, F.Cu at (209.4, 87.8)
- added U35: TXU0202DTTR, ESLGSU_Parts_Lib:SOT833-1-XSON8, F.Cu at (211.9, 87.8)
- added U36: 74LVC2G53GT, ESLGSU_Parts_Lib:SOT833-1-XSON8, F.Cu at (214.3, 87.8)
- added U37: 74LVC2G53GT, ESLGSU_Parts_Lib:SOT833-1-XSON8, F.Cu at (216.8, 87.8)
- added U38: TXU0304RUTR, ESLGSU_Parts_Lib:T-UQFN-12, F.Cu at (214.4, 91.5)
- Q1, Q2, Q3, Q4, Q5, Q6: footprint Package_TO_SOT_SMD:SOT-323_SC-70 -> Package_TO_SOT_SMD:SOT-23
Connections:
- C85 pad 1: Net-(U26-BST) -> Net-(U27-BST)
- C85 pad 2: Net-(U26-SW) -> Net-(U27-SW)
- C89 pad 1: Net-(U27-BST) -> Net-(U26-BST)
- C89 pad 2: Net-(U27-SW) -> Net-(U26-SW)
- C92 pad 1: Net-(U27-EN) -> Net-(U26-EN)
- L5 pad 1: Net-(U26-SW) -> Net-(U27-SW)
- L6 pad 1: Net-(U27-SW) -> Net-(U26-SW)
- U26 pad 1: /SYS_5V -> /SYS_3V3
- U27 pad 1: /SYS_3V3 -> /SYS_5V
- U27 pad 2: Net-(U27-EN) -> Net-(U26-EN)
- U27 pad 3: Net-(U27-EN) -> Net-(U26-EN)
